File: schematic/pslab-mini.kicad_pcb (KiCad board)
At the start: 4 copper layers, 85 x 56 mm, 144 parts, among them J2 BAT, J3 Conn_Coaxial, J4 Conn_Coaxial, J5 Conn_02x16_Odd_Even, J6 Conn_01x15_Socket, J7 Conn_02x03_Top_Bottom, J8 USB_C_Receptacle_USB2.0_16P, Q1 MMBT3904, Q2 MMBT3906, SW1 Reset, SW2 Power, U1 MT2496, U10 TL082, U11 ESP32-C3, U12 IP5189T, U2 AP3015A, U4 SP0503BAHT, U5 AMS1117-3.3, U6 STM32H563RIT6, U7 TL082, U8 MCP6S21, U9 MCP6S21, X1 32kHz768, Y1 Crystal_25MHz, Y2 Crystal_40Mhz

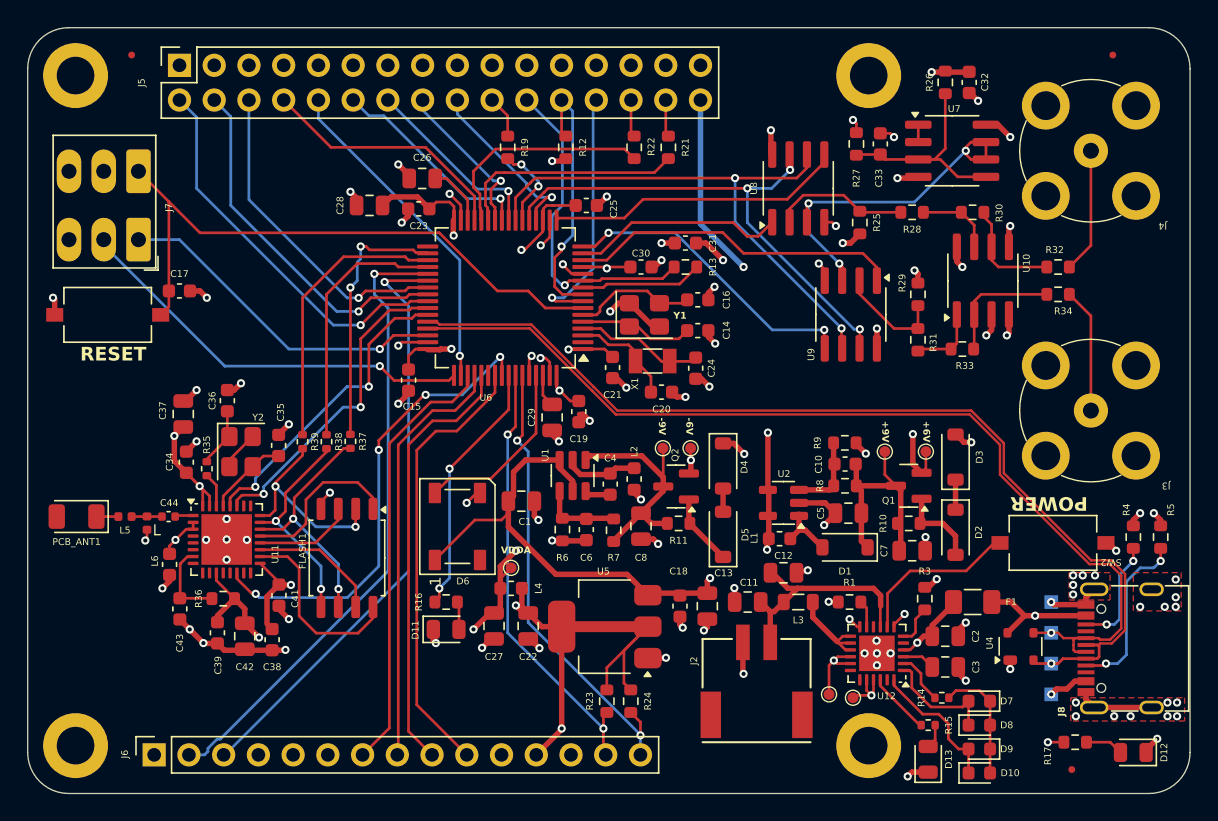
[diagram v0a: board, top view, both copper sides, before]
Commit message: Update layout and routing  (#51)
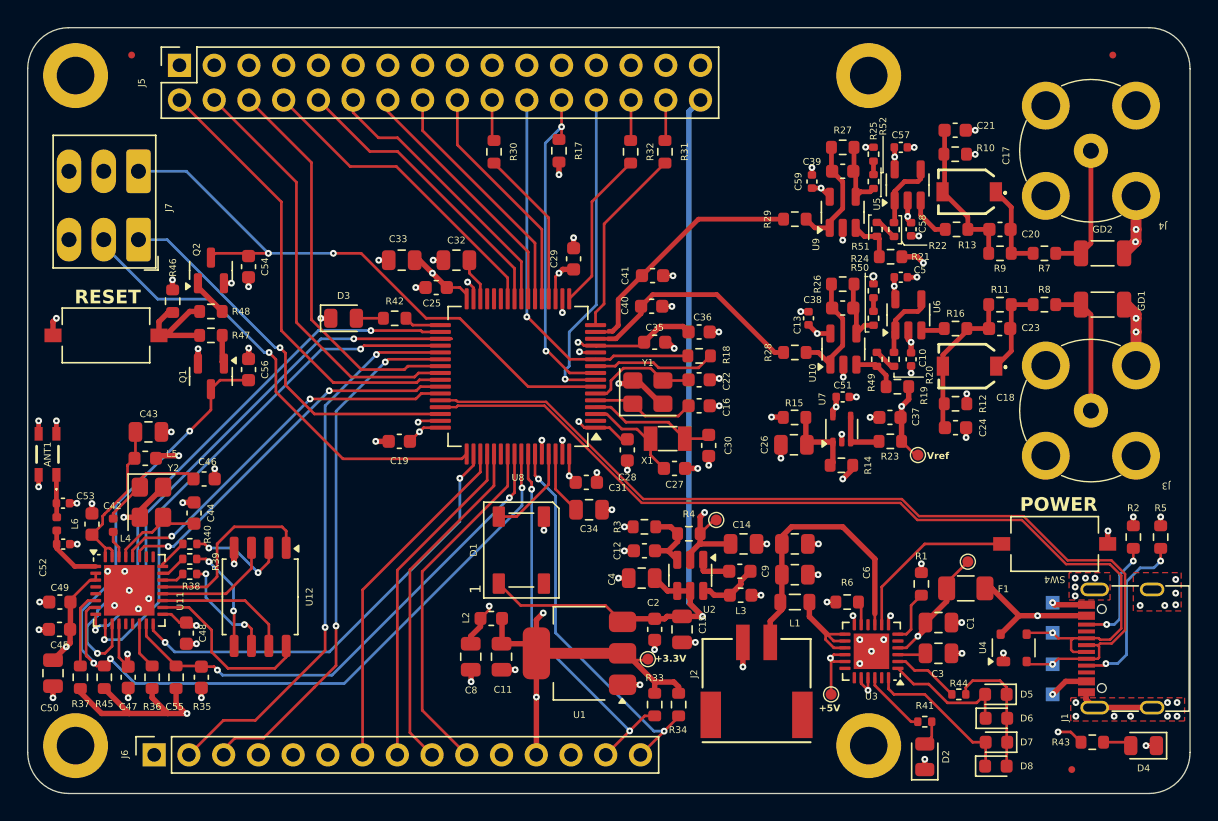
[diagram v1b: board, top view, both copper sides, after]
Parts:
- removed D10: 100%, LED_SMD:LED_0603_1608Metric
- removed D11, D13: GREEN, LED_SMD:LED_0805_2012Metric
- removed D12: BLUE, LED_SMD:LED_0805_2012Metric
- removed D9: 75%, LED_SMD:LED_0603_1608Metric
- removed FLASH1: W25Q32JV, Package_SO:SOIC-8_5.3x5.3mm_P1.27mm
- removed J8: USB_C_Receptacle_USB2.0_16P, pslab-mini:USB_C_Receptacle_G-Switch_GT-USB-7010ASV
- removed PCB_ANT1: ANT, RF_Antenna:Johanson_2450AT18x100
- removed SW2: Power, Button_Switch_SMD:SW_Tactile_SPST_NO_Straight_CK_PTS636Sx25SMTRLFS
- removed TP10: +5V, pslab-mini:Test_Point_0.8mm
- removed TP11: VIN, pslab-mini:Test_Point_0.8mm
- added ANT1: 2450AT18D0100001E, pslab-mini:2450AT18D0100001E, F.Cu at (81.1, 84.5)
- added C45: 100nF, Capacitor_SMD:C_0603_1608Metric, F.Cu at (82.0, 95.2)
- added C46: 10pF, Capacitor_SMD:C_0603_1608Metric, F.Cu at (92.5, 86.2)
- added C47: 100nF, Capacitor_SMD:C_0603_1608Metric, F.Cu at (87.0, 100.8)
- added C48: 1uF, Capacitor_SMD:C_0603_1608Metric, F.Cu at (91.2, 97.5)
- added C49: 1uF, Capacitor_SMD:C_0603_1608Metric, F.Cu at (82.0, 97.2)
- added C50: 10uF, Capacitor_SMD:C_0805_2012Metric, F.Cu at (81.5, 100.5)
- added C51: 100nF, Capacitor_SMD:C_0402_1005Metric, F.Cu at (139.2, 80.2)
- added C52: TBD, Capacitor_SMD:C_0402_1005Metric, F.Cu at (82.2, 91.0)
- added C53: TBD, Capacitor_SMD:C_0402_1005Metric, F.Cu at (82.2, 88.0)
- added C54: 100nF, Capacitor_SMD:C_0603_1608Metric, F.Cu at (95.8, 70.7)
- added C55: 100nF, Capacitor_SMD:C_0603_1608Metric, F.Cu at (92.3, 100.8)
- added C56: 100nF, Capacitor_SMD:C_0603_1608Metric, F.Cu at (95.8, 78.2)
- added C57: 100nF, Capacitor_SMD:C_0402_1005Metric, F.Cu at (143.5, 62.0)
- added C58: 100nF, Capacitor_SMD:C_0402_1005Metric, F.Cu at (144.2, 68.0)
- added C59: 100nF, Capacitor_SMD:C_0402_1005Metric, F.Cu at (137.0, 64.5)
- added C9: 22nF, Capacitor_SMD:C_0603_1608Metric, F.Cu at (131.7, 93.0)
- added GD1: SMD3216-090N, pslab-mini:SMD3216-090N, F.Cu at (158.2, 73.5)
- added GD2: SMD3216-090N, pslab-mini:SMD3216-090N, F.Cu at (158.2, 69.8)
- added J1: USB_C_Receptacle_USB2.0_16P, pslab-mini:USB_C_Receptacle_G-Switch_GT-USB-7010ASV, F.Cu at (160.8, 98.7)
- added R18: 10k, Resistor_SMD:R_0603_1608Metric, F.Cu at (128.8, 77.2)
- added R2: 5k1, Resistor_SMD:R_0603_1608Metric, F.Cu at (160.5, 90.5)
- added R20: 3k, Resistor_SMD:R_0402_1005Metric, F.Cu at (143.0, 77.5)
- added R40: 0, Resistor_SMD:R_0402_1005Metric, F.Cu at (91.5, 91.0)
- added R41: 200, Resistor_SMD:R_0402_1005Metric, F.Cu at (145.2, 104.0)
- added R42: 5k1, Resistor_SMD:R_0603_1608Metric, F.Cu at (106.5, 74.5)
- added R43: 5k1, Resistor_SMD:R_0603_1608Metric, F.Cu at (157.5, 105.5)
- added R44: 200, Resistor_SMD:R_0402_1005Metric, F.Cu at (147.7, 102.0)
- added R45: 10k, Resistor_SMD:R_0603_1608Metric, F.Cu at (85.2, 100.8)
- added R46: 10k, Resistor_SMD:R_0603_1608Metric, F.Cu at (90.2, 73.2)
- added R47: 10k, Resistor_SMD:R_0603_1608Metric, F.Cu at (93.0, 75.8)
- added R48: 10k, Resistor_SMD:R_0603_1608Metric, F.Cu at (93.0, 74.0)
- added R49: 3k, Resistor_SMD:R_0402_1005Metric, F.Cu at (141.8, 77.5)
- added R50: 3k, Resistor_SMD:R_0402_1005Metric, F.Cu at (141.5, 74.5)
- added R51: 3k, Resistor_SMD:R_0402_1005Metric, F.Cu at (141.8, 68.0)
- added R52: 3k, Resistor_SMD:R_0402_1005Metric, F.Cu at (141.5, 64.5)
- added SW4: Power, Button_Switch_SMD:SW_Tactile_SPST_NO_Straight_CK_PTS636Sx25SMTRLFS, F.Cu at (154.8, 91.0)
- added U3: IP5189T, Package_DFN_QFN:QFN-24-1EP_4x4mm_P0.5mm_EP2.6x2.6mm, F.Cu at (141.3, 98.8)
- C10: footprint Capacitor_SMD:C_0603_1608Metric -> Capacitor_SMD:C_0402_1005Metric
- C12: value 22uF -> 12pF; footprint Capacitor_SMD:C_0805_2012Metric -> Capacitor_SMD:C_0603_1608Metric
- C13, C5: value 22uF -> 100nF; footprint Capacitor_SMD:C_0805_2012Metric -> Capacitor_SMD:C_0402_1005Metric
- C14: value 5.6pF -> 22uF; footprint Capacitor_SMD:C_0603_1608Metric -> Capacitor_SMD:C_0805_2012Metric
- C15: value 100nF -> 22uF; footprint Capacitor_SMD:C_0603_1608Metric -> Capacitor_SMD:C_0805_2012Metric
- C17: value 100nF -> 2pF~6pF; footprint Capacitor_SMD:C_0603_1608Metric -> pslab-mini:STC3MA06-T1
- C18: value 1uF -> 2pF~6pF; footprint Capacitor_SMD:C_0603_1608Metric -> pslab-mini:STC3MA06-T1
- C2: value 22uF -> 1uF; footprint Capacitor_SMD:C_0805_2012Metric -> Capacitor_SMD:C_0603_1608Metric
- C20: value 10pF -> 16pF
- C21: value 100nF -> 90pF
- C22: value 10uF -> 5.6pF; footprint Capacitor_SMD:C_0805_2012Metric -> Capacitor_SMD:C_0603_1608Metric
- C23: value 100nF -> 16pF
- C24: value 10pF -> 90pF
- C26: value 2.2uF -> 10uF
- C27: value 22uF -> 10pF; footprint Capacitor_SMD:C_0805_2012Metric -> Capacitor_SMD:C_0603_1608Metric
- C28: value 4.7uF -> 100nF; footprint Capacitor_SMD:C_0805_2012Metric -> Capacitor_SMD:C_0603_1608Metric
- C29: value 2.2uF -> 100nF; footprint Capacitor_SMD:C_0805_2012Metric -> Capacitor_SMD:C_0603_1608Metric
- C30: value 100nF -> 10pF
- C31: value 1uF -> 100nF
- C32: value 100nF -> 2.2uF; footprint Capacitor_SMD:C_0603_1608Metric -> Capacitor_SMD:C_0805_2012Metric
- C33: value 10nF -> 4.7uF; footprint Capacitor_SMD:C_0603_1608Metric -> Capacitor_SMD:C_0805_2012Metric
- C34: value 1uF -> 2.2uF; footprint Capacitor_SMD:C_0603_1608Metric -> Capacitor_SMD:C_0805_2012Metric
- C35: value 10pF -> 100nF
- C36: value 10pF -> 1uF
- C37: value 10uF -> 100nF; footprint Capacitor_SMD:C_0805_2012Metric -> Capacitor_SMD:C_0603_1608Metric
- C38: value 1uF -> 1.2pF
- C39: value 0.1uF -> 1.2pF
- C4: value 22nF -> 22uF; footprint Capacitor_SMD:C_0603_1608Metric -> Capacitor_SMD:C_0805_2012Metric
- C40: value 0.1uF -> 22pF
- C41: value 1uF -> 22pF
- C42: value 10uF -> 1uF; footprint Capacitor_SMD:C_0805_2012Metric -> Capacitor_SMD:C_0603_1608Metric
- C43: value 1uF -> 10uF; footprint Capacitor_SMD:C_0603_1608Metric -> Capacitor_SMD:C_0805_2012Metric
- C44: value 1pF -> 10pF; footprint Capacitor_SMD:C_0402_1005Metric -> Capacitor_SMD:C_0603_1608Metric
- C6: value 12pF -> 22uF; footprint Capacitor_SMD:C_0603_1608Metric -> Capacitor_SMD:C_0805_2012Metric
- C7: value 10uF -> 22uF
- C8: value 22uF -> 10uF
- D1: value K1N5817HW -> WS2812B; footprint Diode_SMD:D_SOD-123 -> LED_SMD:LED_WS2812B_PLCC4_5.0x5.0mm_P3.2mm
- D2: value 1N4148W -> GREEN; footprint Diode_SMD:D_SOD-123 -> LED_SMD:LED_0805_2012Metric
- D3: value 6v8 -> GREEN; footprint Diode_SMD:D_SOD-123 -> LED_SMD:LED_0805_2012Metric
- D4: value 6v8 -> BLUE; footprint Diode_SMD:D_SOD-123 -> LED_SMD:LED_0805_2012Metric
- D5: value 1N4148W -> 25%; footprint Diode_SMD:D_SOD-123 -> LED_SMD:LED_0603_1608Metric
- D6: value WS2812B -> 50%; footprint LED_SMD:LED_WS2812B_PLCC4_5.0x5.0mm_P3.2mm -> LED_SMD:LED_0603_1608Metric
- D7: value 25% -> 75%
- D8: value 50% -> 100%
- FID1: value Fiducial -> TL
- FID2: value Fiducial -> TR
- FID3: value Fiducial -> BL
- L1: value 3.3uH -> 4.7uH; footprint Inductor_SMD:L_0603_1608Metric -> Inductor_SMD:L_0805_2012Metric
- L3: value 4.7uH -> 3.3uH; footprint Inductor_SMD:L_0805_2012Metric -> Inductor_SMD:L_0603_1608Metric
- L4: value 3.3uH -> 24nH; footprint Inductor_SMD:L_0603_1608Metric -> Inductor_SMD:L_0402_1005Metric
- L5: value 3.9nH -> 3.3uH; footprint Inductor_SMD:L_0402_1005Metric -> Inductor_SMD:L_0603_1608Metric
- L6: value 2.7nH -> TBD
- Q2: value MMBT3906 -> MMBT3904
- R1: value 200k -> 51k
- R10: value 1k -> 180k
- R11: value 1k -> 820k
- R12: value 5k1 -> 180k
- R13: value 10k -> 2k
- R14, R15: value 200 -> 10k; footprint Resistor_SMD:R_0402_1005Metric -> Resistor_SMD:R_0603_1608Metric
- R16: value 5k1 -> 2k
- R19, R21: value 200 -> 10k
- R22: value 200 -> 3k; footprint Resistor_SMD:R_0603_1608Metric -> Resistor_SMD:R_0402_1005Metric
- R23: value 5k1 -> 4R7
- R24: value 5k1 -> 3k; footprint Resistor_SMD:R_0603_1608Metric -> Resistor_SMD:R_0402_1005Metric
- R25: value 10k -> 3k; footprint Resistor_SMD:R_0603_1608Metric -> Resistor_SMD:R_0402_1005Metric
- R28, R29: value 10k -> 47R
- R3: value 51k -> 100k
- R30: value 200k -> 200
- R31: value 10k -> 200
- R32: value 1M -> 200
- R33: value 200k -> 5k1
- R34: value 1M -> 5k1
- R35, R37: value 0 -> 10k; footprint Resistor_SMD:R_0402_1005Metric -> Resistor_SMD:R_0603_1608Metric
- R4: value 5k1 -> 42.2k
- R6: value 100k -> 200k
- R7: value 10k -> 10R
- R8: value 180k -> 10R
- R9: value 30k -> 820k
- TP1: value TestPoint -> +3V3
- TP2: value D+ -> USBD-
- TP3: value TestPoint -> USBD+; footprint pslab-mini:Test_Point_0.8mm -> TestPoint:TestPoint_Pad_1.0x1.0mm; moved to B.Cu
- TP4: value D- -> VBUS
- TP5: value TestPoint -> +5V
- TP6: value VINBUS -> -2V; footprint TestPoint:TestPoint_Pad_1.0x1.0mm -> pslab-mini:Test_Point_0.8mm; moved to F.Cu
- TP7: value TestPoint -> VIN
- TP8: value GND -> Vref; footprint TestPoint:TestPoint_Pad_1.0x1.0mm -> pslab-mini:Test_Point_0.8mm; moved to F.Cu
- TP9: value TestPoint -> GND; footprint pslab-mini:Test_Point_0.8mm -> TestPoint:TestPoint_Pad_1.0x1.0mm; moved to B.Cu
- U1: value MT2496 -> AMS1117-3.3; footprint Package_TO_SOT_SMD:SOT-23-6 -> Package_TO_SOT_SMD:SOT-223-3_TabPin2
- U10: value TL082 -> OPA356AIDBVR; footprint Package_SO:SOIC-8_3.9x4.9mm_P1.27mm -> Package_TO_SOT_SMD:SOT-23-5
- U12: value IP5189T -> W25Q32JV; footprint Package_DFN_QFN:QFN-24-1EP_4x4mm_P0.5mm_EP2.6x2.6mm -> Package_SO:SOIC-8_5.3x5.3mm_P1.27mm
- U2: value AP3015A -> MT2496; footprint Package_TO_SOT_SMD:SOT-23-5 -> Package_TO_SOT_SMD:SOT-23-6
- U5: value AMS1117-3.3 -> OPA356AIDBVR; footprint Package_TO_SOT_SMD:SOT-223-3_TabPin2 -> Package_TO_SOT_SMD:SOT-23-5
- U6: value STM32H563RIT6 -> OPA356AIDBVR; footprint Package_QFP:LQFP-64_10x10mm_P0.5mm -> Package_TO_SOT_SMD:SOT-23-5
- U7: value TL082 -> TLV9001IDCK; footprint Package_SO:SOIC-8_3.9x4.9mm_P1.27mm -> Package_TO_SOT_SMD:SOT-353_SC-70-5
- U8: value MCP6S21 -> STM32H563RIT6; footprint Package_SO:SOIC-8_3.9x4.9mm_P1.27mm -> Package_QFP:LQFP-64_10x10mm_P0.5mm
- U9: value MCP6S21 -> OPA356AIDBVR; footprint Package_SO:SOIC-8_3.9x4.9mm_P1.27mm -> Package_TO_SOT_SMD:SOT-23-5
- Y2: value Crystal_40Mhz -> 40MHz
- moved C17 58.2 mm to (148.5, 65.2), turned to 180 degrees
- moved R17 57.4 mm to (118.5, 62.2), turned to -90 degrees
- moved C39 56.8 mm to (139.2, 63.8), turned to 180 degrees
- moved C37 51.7 mm to (142.7, 81.8), turned to 180 degrees
- moved Q1 51.7 mm to (93.0, 78.8), turned to -90 degrees
- moved C38 48.3 mm to (139.2, 73.8), turned to 180 degrees
- moved D3 45.9 mm to (102.8, 74.5), turned to 0 degrees
- moved U12 45.3 mm to (96.7, 94.9), turned to -90 degrees
- moved C23 43.4 mm to (150.7, 75.2)
- moved R16 42.3 mm to (147.5, 75.2)
- moved D6 41.8 mm to (150.5, 103.8), turned to 0 degrees
- moved R34 40.9 mm to (127.2, 102.8), turned to 90 degrees
- moved C40 40.0 mm to (125.3, 73.6), turned to 180 degrees
- moved C32 39.7 mm to (111.0, 70.2), turned to 180 degrees
- moved U5 39.2 mm to (144.0, 64.8), turned to 90 degrees
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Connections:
- C1 pad 1: +5V -> VIN
- C10 pad 1: +9V -> -2V
- C10 pad 2: Net-(U2-FB) -> GND
- C11 pad 1: /BC_BATT -> VDDA
- C12 pad 1: /BC_BATT -> GND
- C12 pad 2: GND -> Net-(U2-FB)
- C13 pad 1: +5V -> +3V3
- C14 pad 1: /HSE_IN -> GND
- C14 pad 2: GND -> -2V
- C15 pad 1: +3V3 -> +5V
- C16 pad 1: /HSE_OUT -> /HSE_IN
- C17 pad 1: /NRST -> Net-(C17-Pad1)
- C17 pad 2: GND -> Net-(C17-Pad2)
- C18 pad 1: GND -> Net-(C18-Pad1)
- C18 pad 2: +5V -> Net-(C18-Pad2)
- C2 pad 1: VIN -> GND
- C2 pad 2: GND -> +5V
- C20 pad 1: /LSE_IN -> Net-(C17-Pad1)
- C20 pad 2: GND -> Net-(C17-Pad2)
- C21 pad 1: +3V3 -> Net-(C17-Pad2)
- C22 pad 1: GND -> /HSE_OUT
- C22 pad 2: +3V3 -> GND
- C23 pad 1: +3V3 -> Net-(C18-Pad1)
- C23 pad 2: GND -> Net-(C18-Pad2)
- C24 pad 1: /LSE_OUT -> Net-(C18-Pad2)
- C26 pad 1: Net-(C26-Pad1) -> Net-(U7-+)
- C27 pad 1: VDDA -> /LSE_IN
- C29 pad 1: Net-(C29-Pad1) -> +3V3
- C30 pad 1: VDDA -> /LSE_OUT
- C31 pad 1: VDDA -> +3V3
- C32 pad 1: VDDA -> Net-(C32-Pad1)
- C33 pad 1: Net-(U7A-+) -> +3V3
- C34 pad 1: VDDA -> Net-(C34-Pad1)
- C35 pad 1: GND -> VDDA
- C35 pad 2: Net-(U11-XTAL_N) -> GND
- C36 pad 1: GND -> VDDA
- C36 pad 2: Net-(C36-Pad2) -> GND
- C37 pad 1: VDDA -> /Vref
- C38 pad 1: +3V3 -> Net-(U10--)
- C38 pad 2: GND -> Net-(C38-Pad2)
- C39 pad 1: +3V3 -> Net-(U9--)
- C39 pad 2: GND -> Net-(C39-Pad2)
- C4 pad 1: Net-(U1-SW) -> +5V
- C4 pad 2: Net-(U1-BS) -> GND
- C40 pad 1: +3V3 -> GND
- C40 pad 2: GND -> /CH1_IN
- C41 pad 1: +3V3 -> GND
- C41 pad 2: GND -> /CH2_IN
- C42 pad 1: +3V3 -> EAVDD
- C43 pad 1: Net-(U11-CHIP_EN) -> EAVDD
- C44 pad 1: /LNA_IN -> GND
- C44 pad 2: Net-(C44-Pad2) -> Net-(U11-XTAL_N)
- C5 pad 1: +9V -> +3V3
- C6 pad 1: GND -> /BC_BATT
- C6 pad 2: Net-(U1-FB) -> GND
- C7 pad 1: +9V -> /BC_BATT
- C8 pad 2: -9V -> +3V3
- D1 pad 1: +9V -> +5V
- D1 pad 2: Net-(D1-A) -> unconnected-(D1-DOUT-Pad2)
- D2 pad 1: Net-(D2-K) -> GND
- D3 pad 1: Net-(D2-K) -> GND
- D3 pad 2: GND -> Net-(D3-A)
- D5 pad 1: Net-(D5-K) -> /BC_LED3R
- D5 pad 2: Net-(D4-A) -> /BC_LED2
- D6 pad 1: +5V -> /BC_LED2
- D6 pad 2: unconnected-(D6-DOUT-Pad2) -> /BC_LED3R
- D7 pad 2: /BC_LED2 -> /BC_LED1
- D8 pad 1: /BC_LED2 -> /BC_LED1
- L1 pad 1: +5V -> /LX
- L1 pad 2: Net-(D1-A) -> /BC_BATT
- L2 pad 1: Net-(U1-SW) -> VDDA
- L2 pad 2: GND -> +3V3
- L3 pad 1: /LX -> Net-(U2-SW)
- L3 pad 2: /BC_BATT -> GND
- L4 pad 1: VDDA -> Net-(C46-Pad2)
- L4 pad 2: +3V3 -> Net-(U11-XTAL_P)
- L5 pad 1: Net-(L5-Pad1) -> +3V3
- L5 pad 2: Net-(C44-Pad2) -> EAVDD
- L6 pad 1: Net-(C44-Pad2) -> /ESP_ANT_IN
- L6 pad 2: GND -> /ESP_ANT
- Q1 pad 1: Net-(D2-A) -> Net-(Q1-B)
- Q1 pad 2: +6V -> GND
- Q1 pad 3: +9V -> /ESP_EN
- Q2 pad 1: Net-(D5-K) -> Net-(Q2-B)
- Q2 pad 2: -6V -> GND
- Q2 pad 3: -9V -> /NRST
- R1 pad 2: /BC_ICHG -> /BC_NTC
- R10 pad 1: Net-(D2-A) -> GND
- R10 pad 2: +9V -> Net-(C17-Pad2)
- R11 pad 1: Net-(D5-K) -> Net-(C18-Pad2)
- R11 pad 2: -9V -> Net-(C18-Pad1)
- R12 pad 1: /RES -> GND
- R12 pad 2: +3V3 -> Net-(C18-Pad2)
- R13 pad 1: /CAP -> Net-(U5-+)
- R13 pad 2: Net-(U6-PC2) -> Net-(C17-Pad2)
- R14 pad 1: /BC_LED3 -> Net-(U7-+)
- R14 pad 2: /BC_LED3R -> VDDA
- R15 pad 1: /BC_LED -> GND
- R15 pad 2: Net-(D13-A) -> Net-(U7-+)
- R16 pad 1: /USER_LED -> Net-(U6-+)
- R16 pad 2: Net-(D11-A) -> Net-(C18-Pad2)
- R17 pad 1: VIN -> /RES
- R17 pad 2: Net-(D12-A) -> +3V3
- R19 pad 1: /FQY -> Net-(U10-+)
- R19 pad 2: Net-(U6-PA6) -> /Vref
- R21 pad 1: /LA2 -> Net-(U9-+)
- R21 pad 2: Net-(U6-PB1) -> /Vref
- R22 pad 1: /LA1 -> /Vatt_2
- R22 pad 2: Net-(U6-PB2) -> Net-(R22-Pad2)
- R23 pad 1: /I2C1_SCL -> Net-(U7--)
- R23 pad 2: +3V3 -> /Vref
- R24 pad 1: /I2C1_SDA -> GND
- R24 pad 2: +3V3 -> Net-(R24-Pad2)
- R25 pad 1: VDDA -> GND
- R25 pad 2: Net-(U8-CHA) -> Net-(R25-Pad2)
- R26 pad 1: Net-(U7A-+) -> Net-(U10--)
- R26 pad 2: VDDA -> Net-(C38-Pad2)
- R27 pad 1: Net-(U7A-+) -> Net-(U9--)
- R27 pad 2: GND -> Net-(C39-Pad2)
- R28 pad 1: Net-(R28-Pad1) -> Net-(C38-Pad2)
- R28 pad 2: Net-(U8-CHA) -> /CH1_IN
- R29 pad 1: VDDA -> Net-(C39-Pad2)
- R29 pad 2: Net-(U9-CHA) -> /CH2_IN
- R3 pad 2: /BC_NTC -> Net-(U2-FB)
- R30 pad 1: Net-(R28-Pad1) -> /FQY
- R30 pad 2: Net-(U10B--) -> Net-(U8-PA4)
- R31 pad 1: Net-(R31-Pad1) -> /LA2
- R31 pad 2: Net-(U9-CHA) -> Net-(U8-PA2)
- R32 pad 1: /CH2 -> /LA1
- R32 pad 2: Net-(U10B--) -> Net-(U8-PA3)
- R33 pad 1: Net-(U10A--) -> /I2C1_SCL
- R33 pad 2: Net-(R31-Pad1) -> +3V3
- R34 pad 1: Net-(U10A--) -> /I2C1_SDA
- R34 pad 2: /CH1 -> +3V3
- R35 pad 1: Net-(C36-Pad2) -> /ESP_{BOOT}
- R35 pad 2: Net-(U11-XTAL_P) -> +3V3
- R36 pad 1: Net-(U11-CHIP_EN) -> /ESP_STRAP_2
- R37 pad 1: /SPI2_SCK -> /ESP_STRAP_1
- R37 pad 2: /SPICLK -> +3V3
- R38 pad 1: /SPI2_MOSI -> /ESP_SPI_CLK
- R38 pad 2: /SPID -> Net-(U11-SPICLK)
- R39 pad 1: /SPI2_MISO -> Net-(U11-SPID)
- R39 pad 2: /SPIQ -> /ESP_SPI_MOSI
- R4 pad 1: GND -> Net-(U2-FB)
- R4 pad 2: Net-(J8-CC2) -> -2V
- R6 pad 2: Net-(U1-FB) -> /BC_ICHG
- R7 pad 1: Net-(U1-FB) -> Net-(C17-Pad1)
- R7 pad 2: -9V -> /CH2
- R8 pad 1: +9V -> Net-(C18-Pad1)
- R8 pad 2: Net-(U2-FB) -> /CH1
- R9 pad 1: Net-(U2-FB) -> Net-(C17-Pad2)
- R9 pad 2: GND -> Net-(C17-Pad1)
- SW1 pad 1: /NRST -> Net-(R46-Pad1)
- SW1 pad 2: GND -> +3V3
- TP1 pad 1: VDDA -> +3V3
- TP2 pad 1: VBUS -> /D-
- TP3 pad 1: -9V -> /D+
- TP4 pad 1: /D+ -> VBUS
- TP5 pad 1: -6V -> +5V
- TP6 pad 1: /D- -> -2V
- TP7 pad 1: +9V -> VIN
- TP8 pad 1: GND -> /Vref
- TP9 pad 1: +6V -> GND
- U1 pad 1: -9V -> GND
- U1 pad 2: Net-(U1-SW) -> +3V3
- U10 pad 1: Net-(R31-Pad1) -> Net-(C38-Pad2)
- U10 pad 2: Net-(U10A--) -> GND
- U10 pad 3: GND -> Net-(U10-+)
- U10 pad 4: -6V -> Net-(U10--)
- U10 pad 5: GND -> +3V3
- U11 pad 1: /LNA_IN -> /ESP_ANT
- U11 pad 10: unconnected-(U11-MTDI-Pad10) -> /ESP_SPI2_CLK
- U11 pad 14: /ESP_DATA_READY -> /ESP_STRAP_2
- U11 pad 15: unconnected-(U11-GPIO9-Pad15) -> /ESP_{BOOT}
- U11 pad 16: unconnected-(U11-GPIO10-Pad16) -> /ESP_DATA_READY
- U11 pad 19: /SPIHD -> /ESP_FLASH_RST
- U11 pad 20: /SPIWP -> /ESP_FLASH_WP
- U11 pad 21: /SPICS0 -> /ESP_FLASH_CS
- U11 pad 22: /SPICLK -> Net-(U11-SPICLK)
- U11 pad 23: /SPID -> Net-(U11-SPID)
- U11 pad 24: /SPIQ -> Net-(U11-SPIQ)
- U11 pad 27: /UART1_TX -> /ESP_UART_TX
- U11 pad 28: /UART1_RX -> /ESP_UART_RX
- U11 pad 31: VDDA -> EAVDD
- U11 pad 32: VDDA -> EAVDD
- U11 pad 6: unconnected-(U11-GPIO2-Pad6) -> /ESP_STRAP_1
- U11 pad 7: Net-(U11-CHIP_EN) -> /ESP_EN
- U11 pad 8: unconnected-(U11-GPIO3-Pad8) -> /ESP_SPI2_MISO
- U11 pad 9: unconnected-(U11-MTMS-Pad9) -> /ESP_SPI2_MOSI
- U12 pad 1: /BC_LED2 -> /ESP_FLASH_CS
- U12 pad 2: /BC_LED3 -> /ESP_SPI_MISO
- U12 pad 3: /BC_VDD -> /ESP_FLASH_WP
- U12 pad 4: VIN -> GND
- U12 pad 5: unconnected-(U12-RSET-Pad5) -> /ESP_SPI_MOSI
- U12 pad 6: /BC_NTC -> /ESP_SPI_CLK
- U12 pad 7: GND -> /ESP_FLASH_RST
- U12 pad 8: /BC_KEY -> VDD_SPI
- U2 pad 1: Net-(D1-A) -> Net-(U2-BS)
- U2 pad 2: GND -> -2V
- U5 pad 1: GND -> /Vatt_2
- U5 pad 2: +3V3 -> -2V
- U5 pad 3: +5V -> Net-(U5-+)
- U6 pad 1: +3V3 -> /Vatt_1
- U6 pad 2: unconnected-(U6-PC13-Pad2) -> -2V
- U6 pad 3: /LSE_IN -> Net-(U6-+)
- U6 pad 4: /LSE_OUT -> /Vatt_1
- U6 pad 5: /HSE_IN -> +3V3
- U7 pad 1: Net-(U7A--) -> Net-(U7-+)
- U7 pad 2: Net-(U7A--) -> GND
- U7 pad 3: Net-(U7A-+) -> Net-(U7--)
- U7 pad 4: -6V -> Net-(U7--)
- U7 pad 5: Net-(U7A-+) -> +3V3
- U8 pad 1: /CH2_IN -> +3V3
- U8 pad 2: Net-(U8-CHA) -> unconnected-(U8-PC13-Pad2)
- U8 pad 3: /OSC_REF1 -> /LSE_IN
- U8 pad 4: GND -> /LSE_OUT
- U8 pad 5: /CS2 -> /HSE_IN
- U8 pad 6: /SPI1_MOSI -> /HSE_OUT
- U8 pad 7: /SPI1_SCK -> /NRST
- U8 pad 8: VDDA -> /VOL
- U9 pad 1: /CH1_IN -> Net-(C39-Pad2)
- U9 pad 2: Net-(U9-CHA) -> GND
- U9 pad 3: /OSC_REF1 -> Net-(U9-+)
- U9 pad 4: GND -> Net-(U9--)
- U9 pad 5: /CS1 -> +3V3
- Y2 pad 1: Net-(C36-Pad2) -> Net-(C46-Pad2)
- Y2 pad 2: Net-(Y2-Pad2) -> GND
- Y2 pad 4: Net-(Y2-Pad2) -> GND
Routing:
- net +3V3: track 218.2 -> 323.4 mm, vias 11 -> 19
- net VDDA: track 143.8 -> 66.7 mm, vias 11 -> 3
- net /ESP_EN: track 0.00 -> 73.8 mm, vias 0 -> 4
- net -6V: track 58.6 -> 0.00 mm, vias 3 -> 0
- net /ESP_SPI2_CLK: track 0.00 -> 42.9 mm, vias 0 -> 2
- net -2V: track 0.00 -> 41.5 mm, vias 0 -> 3
- net /SPI1_MOSI: track 40.5 -> 0.00 mm, vias 2 -> 0
- net /ESP_SPI2_MISO: track 0.00 -> 40.0 mm, vias 0 -> 2
- net /ESP_SPI2_MOSI: track 0.00 -> 38.5 mm, vias 0 -> 2
- net /SPI1_SCK: track 37.7 -> 0.00 mm, vias 3 -> 0
- net +6V: track 37.4 -> 0.00 mm, vias 3 -> 0
- net /ESP_{BOOT}: track 0.00 -> 37.4 mm, vias 0 -> 2
- net /ESP_UART_RX: track 0.00 -> 27.7 mm, vias 0 -> 2
- net /ESP_UART_TX: track 0.00 -> 27.4 mm, vias 0 -> 2
- net /OSC_REF1: track 26.2 -> 0.00 mm, vias 3 -> 0
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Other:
- board text added: "+3.3V"
- board text added: "+5V"
- board text added: "VBUS"
- board text added: "Vref"
- board text removed: "+6V"
- board text removed: "+9V"
- board text removed: "-6V"
- board text removed: "-9V"
- board text removed: "VDDA"
- board text removed: "VUSBIN"

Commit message: feat: Added logos and labels
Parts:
- added Z1: PSLab logo back, pslab-mini:logo_pslab.io, B.Cu at (117.1, 81.3)
- added Z10: Barcode, pslab-mini:Barcode, B.Cu at (139.7, 81.4)
- added Z11: QR Code, pslab-mini:Website_QR, B.Cu at (107.3, 81.4)
- added Z2: Fossasia logo back, pslab-mini:logo_fossasia, B.Cu at (94.0, 81.8)
- added Z3: OpnTec logo back, pslab-mini:logo_opntec, F.Cu at (99.8, 72.7)
- added Z4: OpenHardware, pslab-mini:logo_open_source_hardware, B.Cu at (128.6, 81.2)
- added Z5: eWaste, pslab-mini:logo_eWaste, B.Cu at (84.9, 77.9)
- added Z6: ESD_logo, Symbol:ESD-Logo_6.6x6mm_SilkScreen, F.Cu at (93.9, 64.6)
- added Z7: PSLab logo front, pslab-mini:logo_pslab.io, F.Cu at (100.0, 85.2)
- added Z8: Fossasia logo front, pslab-mini:logo_fossasia, F.Cu at (106.4, 94.8)
- added Z9: OpnTec logo front, pslab-mini:logo_opntec, B.Cu at (97.9, 81.7)
- moved D3 1.38 mm to (103.7, 73.5), turned to -90 degrees
- moved R17 0.25 mm to (118.5, 62.5)
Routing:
- net +3V3: track 323.4 -> 322.3 mm
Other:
- board text added: "+3V3"
- board text added: "1"
- board text added: "30.09.2025"
- board text added: "Analog"
- board text added: "CS for SPI"
- board text added: "Capacitance"
- board text added: "Digital"
- board text added: "Frequency"
- board text added: "GPIO0"
- board text added: "GPIO1"
- board text added: "GPIO2"
- board text added: "GPIO3"
- board text added: "GPIO4"
- board text added: "GPIO5"
- board text added: "GPIO6"
- board text added: "GPIO7"
- board text added: "GPIO8"
- board text added: "GROUND"
- board text added: "Ground"
- board text added: "Logic Analyser 1"
- board text added: "Logic Analyser 2"
- board text added: "MISO for SPI"
- board text added: "MOSI for SPI"
- board text added: "Mini Version"
- board text added: "NRST"
- board text added: "Oscilloscope Channel 1"
- board text added: "Oscilloscope Channel 2"
- board text added: "PSLab"
- board text added: "Pocket Science Lab"
- board text added: "Resistance"
- board text added: "SCK for SPI"
- board text added: "SCL for I2C"
- board text added: "SDA for I2C"
- board text added: "SWCLK"
- board text added: "SWDIO"
- board text added: "UART RX"
- board text added: "UART TX"
- board text added: "VCC(+5V)"
- board text added: "VDD(+3V3)"
- board text added: "Voltage"
- board text added: "https://pslab.io"

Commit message: silkscreen update
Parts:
- moved Z7 1.00 mm to (99.9, 84.2)
- moved Z8 0.85 mm to (107.0, 95.4)
- moved Z2 0.81 mm to (93.2, 81.7)
- moved Z1 0.62 mm to (116.5, 81.2)
- moved Z9 0.40 mm to (97.5, 81.7)
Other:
- board text added: "CAP"
- board text added: "CH1"
- board text added: "CH2"
- board text added: "CS"
- board text added: "FREQ"
- board text added: "I2C"
- board text added: "LA1"
- board text added: "LA2"
- board text added: "MISO"
- board text added: "MOSI"
- board text added: "Mini"
- board text added: "Multimeter"
- board text added: "RES"
- board text added: "RX"
- board text added: "SCK"
- board text added: "SCL"
- board text added: "SDA"
- board text added: "SPI"
- board text added: "TX"
- board text added: "UART"
- board text added: "VOL"
- board text added: "Version"
- board text removed: "CS for SPI"
- board text removed: "Capacitance"
- board text removed: "Frequency"
- board text removed: "Ground"
- board text removed: "Logic Analyser 1"
- board text removed: "Logic Analyser 2"
- board text removed: "MISO for SPI"
- board text removed: "MOSI for SPI"
- board text removed: "Mini Version"
- board text removed: "Oscilloscope Channel 1"
- board text removed: "Oscilloscope Channel 2"
- board text removed: "Resistance"
- board text removed: "SCK for SPI"
- board text removed: "SCL for I2C"
- board text removed: "SDA for I2C"
- board text removed: "UART RX"
- board text removed: "UART TX"
- board text removed: "Voltage"

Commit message: fixup
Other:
- board text added: "+3.3"
- board text added: "VDD(+3.3V)"
- board text removed: "+3V3"
- board text removed: "VDD(+3V3)"
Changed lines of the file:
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@@
 		(sheetname "/")
 		(sheetfile "pslab-mini.kicad_sch")
-		(attr through_hole)
+		(attr through_hole exclude_from_bom)
 		(fp_poly
 			(pts
@@
 		(sheetname "/")
 		(sheetfile "pslab-mini.kicad_sch")
-		(attr exclude_from_pos_files allow_missing_courtyard)
+		(attr exclude_from_pos_files exclude_from_bom allow_missing_courtyard)
 		(fp_poly
 			(pts
@@
 		(sheetname "/")
 		(sheetfile "pslab-mini.kicad_sch")
-		(attr board_only exclude_from_pos_files)
+		(attr board_only exclude_from_pos_files exclude_from_bom)
 		(fp_poly
 			(pts
@@
 		(sheetname "/")
 		(sheetfile "pslab-mini.kicad_sch")
-		(attr board_only exclude_from_pos_files)
+		(attr board_only exclude_from_pos_files exclude_from_bom)
 		(fp_poly
 			(pts
@@
 		(sheetname "/")
 		(sheetfile "pslab-mini.kicad_sch")
-		(attr through_hole)
+		(attr through_hole exclude_from_bom)
 		(fp_poly
 			(pts
@@
 		(sheetname "/")
 		(sheetfile "pslab-mini.kicad_sch")
-		(attr board_only exclude_from_pos_files)
+		(attr board_only exclude_from_pos_files exclude_from_bom)
 		(fp_poly
 			(pts
@@
 		(sheetname "/")
 		(sheetfile "pslab-mini.kicad_sch")
-		(attr board_only exclude_from_pos_files)
+		(attr board_only exclude_from_pos_files exclude_from_bom)
 		(fp_poly
 			(pts
@@
 		(sheetname "/")
 		(sheetfile "pslab-mini.kicad_sch")
-		(attr through_hole)
+		(attr through_hole exclude_from_bom)
 		(fp_poly
 			(pts
@@
 		(sheetname "/")
 		(sheetfile "pslab-mini.kicad_sch")
-		(attr through_hole)
+		(attr through_hole exclude_from_bom)
 		(fp_poly
 			(pts
@@
 		(sheetname "/")
 		(sheetfile "pslab-mini.kicad_sch")
-		(attr board_only exclude_from_pos_files)
+		(attr board_only exclude_from_pos_files exclude_from_bom)
 		(fp_poly
 			(pts
@@
 		(sheetname "/")
 		(sheetfile "pslab-mini.kicad_sch")
-		(attr board_only exclude_from_pos_files)
+		(attr board_only exclude_from_pos_files exclude_from_bom)
 		(fp_poly
 			(pts
@@
 		)
 	)
-	(gr_text "+3V3\n"
-		(at 84.7 62.2 270)
+	(gr_text "+3.3"
+		(at 84.7 62.3 270)
 		(layer "B.SilkS")
 		(effects
@@
 		)
 	)
-	(gr_text "VDD(+3V3)"
+	(gr_text "VDD(+3.3V)"
 		(at 116.3 105.1 270)
 		(layer "B.SilkS")
@@
 	)
 	(gr_text "GND"
-		(at 82.1 62.1 270)
+		(at 82 62.3 270)
 		(layer "B.SilkS")
 		(effects
@@
 	)
 	(gr_text "SWCLK"
-		(at 84.6 75.9 270)
+		(at 84.6 75.6 270)
 		(layer "B.SilkS")
 		(effects
@@
 	)
 	(gr_text "SWDIO"
-		(at 87.3 75.6 270)
+		(at 87.2 75.3 270)
 		(layer "B.SilkS")
 		(effects
@@
 	)
 	(gr_text "NRST\n"
-		(at 87.4 62 270)
+		(at 87.2 62.3 270)
 		(layer "B.SilkS")
 		(effects
@@
 		)
 	)
-	(gr_text "VDD(+3V3)"
+	(gr_text "VDD(+3.3V)"
 		(at 98.4 105.1 270)
 		(layer "B.SilkS")
@@
 		)
 	)
-	(dimension
-		(type orthogonal)
-		(layer "B.SilkS")
-		(pts
-			(xy 82.65 109.25) (xy 82.65 53.25)
-		)
-		(height -5.05)
-		(orientation 1)
-		(format
-			(prefix "")
-			(suffix "")
-			(units 3)
-			(units_format 0)
-			(precision 4)
-			(suppress_zeroes yes)
-		)
-		(style
-			(thickness 0.1)
-			(arrow_length 1.27)
-			(text_position_mode 0)
-			(arrow_direction outward)
-			(extension_height 0.58642)
-			(extension_offset 0.5)
-			(keep_text_aligned yes)
-		)
-		(gr_text "56"
-			(at 77 81.25 90)
-			(layer "B.SilkS")
-			(effects
-				(font
-					(size 0.5 0.5)
-					(thickness 0.1)
-				)
-				(justify mirror)
-			)
-		)
-	)

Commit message: fixup
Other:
- board text added: "Analyser"
- board text added: "Logic"
- board text removed: "VCC(+5V)"
- board text removed: "VDD(+3.3V)"
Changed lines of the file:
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@@
+	)
+	(gr_line
+		(start 123.7 64.9)
+		(end 126.3 64.9)
+		(stroke
+			(width 0.1)
+			(type default)
+		)
+		(layer "B.SilkS")
+	)
+	(gr_line
+		(start 126.3 64.9)
+		(end 126.5 64.9)
+		(stroke
+			(width 0.1)
+			(type default)
+		)
+		(layer "B.SilkS")
 	)
 	(gr_line
@@
 	)
 	(gr_line
-		(start 126.4 65)
-		(end 126.4 63.6)
+		(start 121.4 65)
+		(end 121.4 63.6)
 		(stroke
 			(width 0.1)
@@
 	(gr_line
 		(start 113.7 65)
-		(end 126.4 65)
+		(end 121.4 65)
 		(stroke
 			(width 0.1)
@@
 		(start 130.3 57.3)
 		(end 89.2 57.3)
+		(stroke
+			(width 0.1)
+			(type default)
+		)
+		(layer "B.SilkS")
+	)
+	(gr_line
+		(start 126.5 64.9)
+		(end 126.5 63.5)
 		(stroke
 			(width 0.1)
@@
 		(layer "B.SilkS")
 	)
+	(gr_line
+		(start 123.7 63.5)
+		(end 123.7 64.9)
+		(stroke
+			(width 0.1)
+			(type default)
+		)
+		(layer "B.SilkS")
+	)
 	(gr_rect
 		(start 95.5 100.2)
@@
 	)
 	(gr_text "Multimeter"
-		(at 123.7 66.7 0)
-		(layer "B.SilkS")
-		(effects
-			(font
-				(size 1 1)
-				(thickness 0.2)
-				(bold yes)
-			)
-			(justify left bottom mirror)
-		)
-	)
-	(gr_text "VDD(+3.3V)"
-		(at 116.3 105.1 270)
+		(at 121.6 66.8 0)
+		(layer "B.SilkS")
+		(effects
+			(font
+				(size 1 1)
+				(thickness 0.2)
+				(bold yes)
+			)
+			(justify left bottom mirror)
+		)
+	)
+	(gr_text "+3.3V"
+		(at 116.3 105.3 270)
 		(layer "B.SilkS")
 		(effects
@@
 		)
 	)
-	(gr_text "VCC(+5V)\n"
-		(at 128.3 67.2 270)
+	(gr_text "+5V"
+		(at 128.2 63.2 270)
 		(layer "B.SilkS")
 		(effects
@@
 		)
 	)
+	(gr_text "Logic"
+		(at 127.1 66.7 0)
+		(layer "B.SilkS")
+		(effects
+			(font
+				(size 1 1)
+				(thickness 0.2)
+				(bold yes)
+			)
+			(justify left bottom mirror)
+		)
+	)
 	(gr_text "SWDIO"
 		(at 87.2 75.3 270)
@@
 		)
 	)
+	(gr_text "Analyser"
+		(at 128.3 68.5 0)
+		(layer "B.SilkS")
+		(effects
+			(font
+				(size 1 1)
+				(thickness 0.2)
+				(bold yes)
+			)
+			(justify left bottom mirror)
+		)
+	)
 	(gr_text "NRST\n"
 		(at 87.2 62.3 270)
@@
 		)
 	)
-	(gr_text "VDD(+3.3V)"
-		(at 98.4 105.1 270)
-		(layer "B.SilkS")
-		(effects
+	(gr_text "+3.3V"
+		(at 98.4 105.4 270)
+		(layer "B.SilkS")
+		(effects
